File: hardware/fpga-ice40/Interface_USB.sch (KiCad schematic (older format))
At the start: 16 parts, among them J5 USB_B_Micro, U11 USBLC6-2SC6, U9 FT245RL

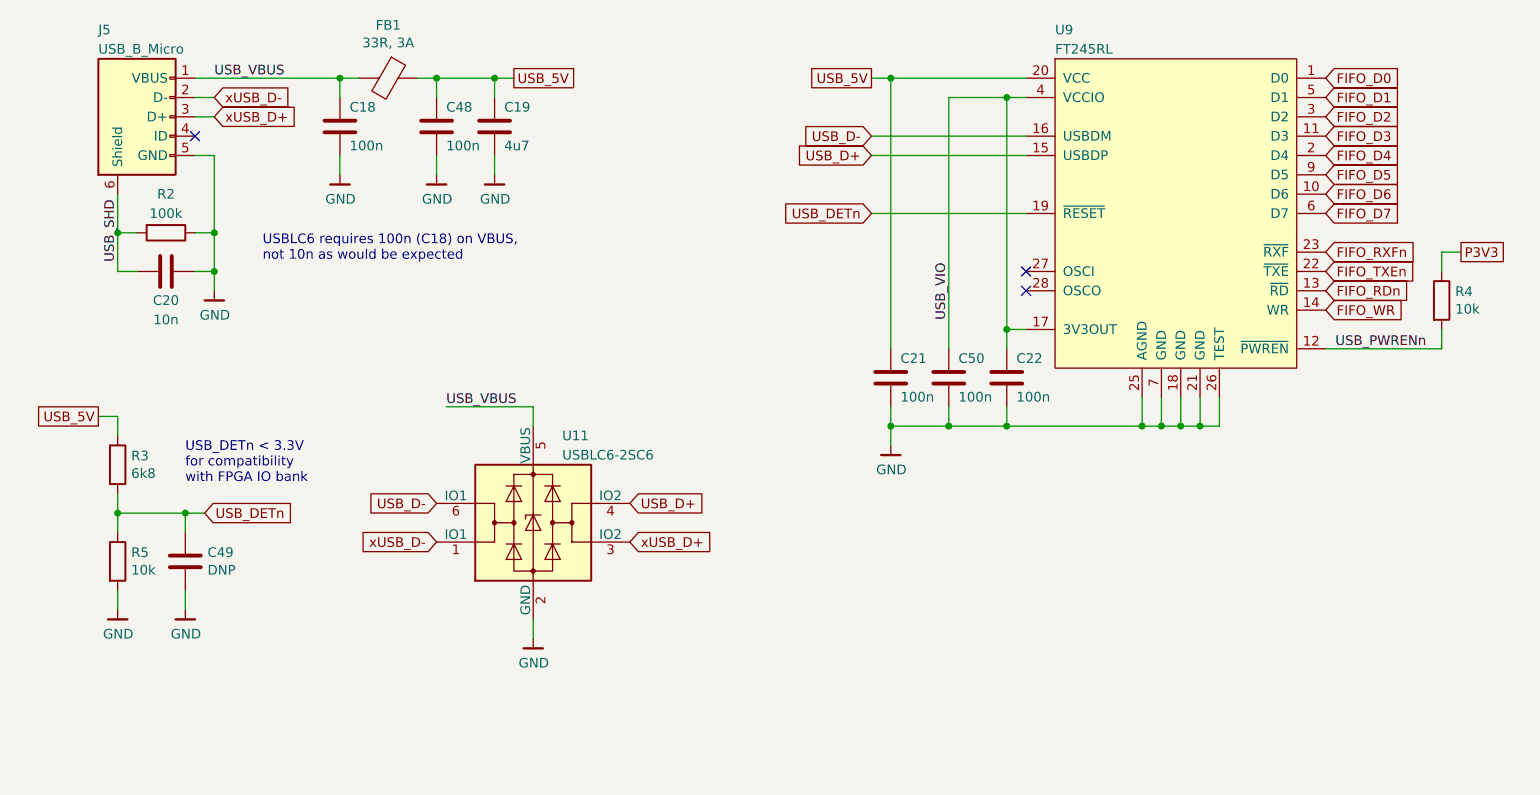
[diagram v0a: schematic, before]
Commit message: Beginning layout of power muxing module
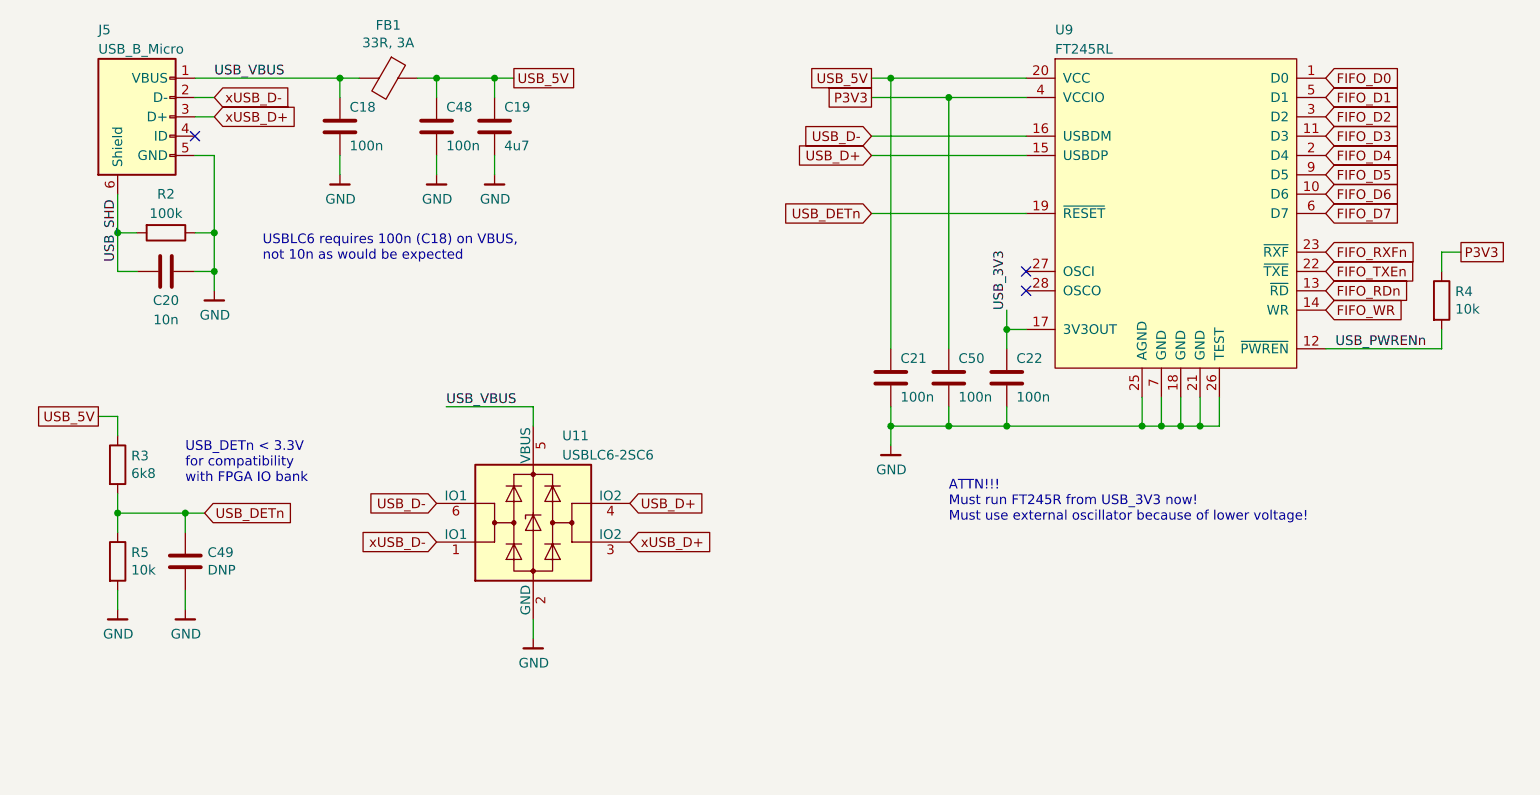
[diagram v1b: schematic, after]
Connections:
- net P3V3: now also C50.1, U9.4 (VCCIO)
- net USB_VIO renamed USB_3V3
- net USB_3V3: no longer C50.1, U9.4 (VCCIO)
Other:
- note added: "ATTN!!!\nMust run FT245R from USB_3V3 now!\nMust use external oscillator because of lower voltage!"
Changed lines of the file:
@@
 Wire Wire Line
 	8000 4250 8100 4250
-$Comp
-L ng_power:GND #PWR?
-U 1 1 5F314866
-P 6400 4350
-AR Path="/5F314866" Ref="#PWR?"  Part="1"
-AR Path="/5F302051/5F314866" Ref="#PWR025"  Part="1"
-F 0 "#PWR025" H 6400 4100 50  0001 C CNN
-F 1 "GND" H 6403 4224 50  0000 C CNN
-F 2 "" H 6300 4000 50  0001 C CNN
-F 3 "" H 6400 4350 50  0001 C CNN
-	1    6400 4350
-	1    0    0    -1
-$EndComp
-Wire Wire Line
-	6400 4350 6400 4250
 NoConn ~ 7100 3450
 NoConn ~ 7100 3550
@@
 	1    0    0    -1
 $EndComp
-Text GLabel 6300 2750 0    50   Input ~ 0
-USB_D-
-Text GLabel 6300 2850 0    50   Input ~ 0
-USB_D+
 Text GLabel 8650 2450 2    50   Input ~ 0
 FIFO_D0
@@
 Wire Wire Line
 	9250 3450 9250 3350
-Wire Wire Line
-	7000 2550 7100 2550
 Text GLabel 9350 3350 2    50   UnSpc ~ 0
 P3V3
 Wire Wire Line
 	9250 3350 9350 3350
-Wire Wire Line
-	7000 3750 7000 2550
-Connection ~ 7000 3750
-Wire Wire Line
-	6300 2750 7100 2750
-Wire Wire Line
-	6300 2850 7100 2850
-Wire Wire Line
-	6300 2450 6400 2450
-Text GLabel 6300 2450 0    50   UnSpc ~ 0
-USB_5V
-Wire Wire Line
-	6300 3150 7100 3150
-Text GLabel 6300 3150 0    50   Input ~ 0
-USB_DETn
-Text Label 6700 3700 1    50   ~ 0
-USB_VIO
 Text Label 8700 3850 0    50   ~ 0
 USB_PWRENn
@@
 Text GLabel 2850 4700 2    50   Input ~ 0
 USB_DETn
-$Comp
-L Device:C C?
-U 1 1 5F3148C7
-P 6400 4000
-AR Path="/5F3148C7" Ref="C?"  Part="1"
-AR Path="/5F302051/5F3148C7" Ref="C21"  Part="1"
-F 0 "C21" H 6450 4100 50  0000 L CNN
-F 1 "100n" H 6450 3900 50  0000 L CNN
-F 2 "Capacitor_SMD:C_0603_1608Metric" H 6438 3850 50  0001 C CNN
-F 3 "~" H 6400 4000 50  0001 C CNN
-F 4 "CL10B104KB8NNNC" H 6400 4000 50  0001 C CNN "MPN"
-	1    6400 4000
-	1    0    0    -1
-$EndComp
-Wire Wire Line
-	6400 3850 6400 2450
-Connection ~ 6400 2450
-Wire Wire Line
-	6400 2450 7100 2450
-Wire Wire Line
-	6400 4150 6400 4250
-Wire Wire Line
-	6400 4250 6700 4250
-Connection ~ 6400 4250
 Wire Wire Line
 	7000 4250 7700 4250
@@
 	1    0    0    -1
 $EndComp
+Wire Wire Line
+	6700 2550 7100 2550
+Connection ~ 7000 4250
+Wire Wire Line
+	6700 3850 6700 2550
+Wire Wire Line
+	6700 4250 7000 4250
+Wire Wire Line
+	6700 4150 6700 4250
 $Comp
 L Device:C C?
@@
 	1    0    0    -1
 $EndComp
-Connection ~ 7000 4250
-Wire Wire Line
-	6700 4150 6700 4250
+Connection ~ 6700 2550
 Connection ~ 6700 4250
 Wire Wire Line
-	6700 4250 7000 4250
-Wire Wire Line
-	6700 3850 6700 2550
-Wire Wire Line
-	6700 2550 7000 2550
-Connection ~ 7000 2550
+	6300 2550 6700 2550
+Text GLabel 6300 2550 0    50   UnSpc ~ 0
+P3V3
+Connection ~ 6400 4250
+Wire Wire Line
+	6400 4250 6700 4250
+Wire Wire Line
+	6400 4150 6400 4250
+Wire Wire Line
+	6400 2450 7100 2450
+Connection ~ 6400 2450
+Wire Wire Line
+	6400 3850 6400 2450
+$Comp
+L Device:C C?
+U 1 1 5F3148C7
+P 6400 4000
+AR Path="/5F3148C7" Ref="C?"  Part="1"
+AR Path="/5F302051/5F3148C7" Ref="C21"  Part="1"
+F 0 "C21" H 6450 4100 50  0000 L CNN
+F 1 "100n" H 6450 3900 50  0000 L CNN
+F 2 "Capacitor_SMD:C_0603_1608Metric" H 6438 3850 50  0001 C CNN
+F 3 "~" H 6400 4000 50  0001 C CNN
+F 4 "CL10B104KB8NNNC" H 6400 4000 50  0001 C CNN "MPN"
+	1    6400 4000
+	1    0    0    -1
+$EndComp
+Text GLabel 6300 2450 0    50   UnSpc ~ 0
+USB_5V
+Wire Wire Line
+	6300 2450 6400 2450
+Wire Wire Line
+	6400 4350 6400 4250
+$Comp
+L ng_power:GND #PWR?
+U 1 1 5F314866
+P 6400 4350
+AR Path="/5F314866" Ref="#PWR?"  Part="1"
+AR Path="/5F302051/5F314866" Ref="#PWR025"  Part="1"
+F 0 "#PWR025" H 6400 4100 50  0001 C CNN
+F 1 "GND" H 6403 4224 50  0000 C CNN
+F 2 "" H 6300 4000 50  0001 C CNN
+F 3 "" H 6400 4350 50  0001 C CNN
+	1    6400 4350
+	1    0    0    -1
+$EndComp
+Text Label 7000 3650 1    50   ~ 0
+USB_3V3
+Wire Wire Line
+	6300 3150 7100 3150
+Text GLabel 6300 3150 0    50   Input ~ 0
+USB_DETn
+Wire Wire Line
+	6300 2850 7100 2850
+Text GLabel 6300 2850 0    50   Input ~ 0
+USB_D+
+Wire Wire Line
+	6300 2750 7100 2750
+Text GLabel 6300 2750 0    50   Input ~ 0
+USB_D-
+Wire Wire Line
+	7000 3650 7000 3750
+Connection ~ 7000 3750
+Text Notes 6700 4750 0    50   ~ 0
+ATTN!!!\nMust run FT245R from USB_3V3 now!\nMust use external oscillator because of lower voltage!
 $EndSCHEMATC

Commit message: Swtich USB interface to P3V3 and add 12MHz oscillator
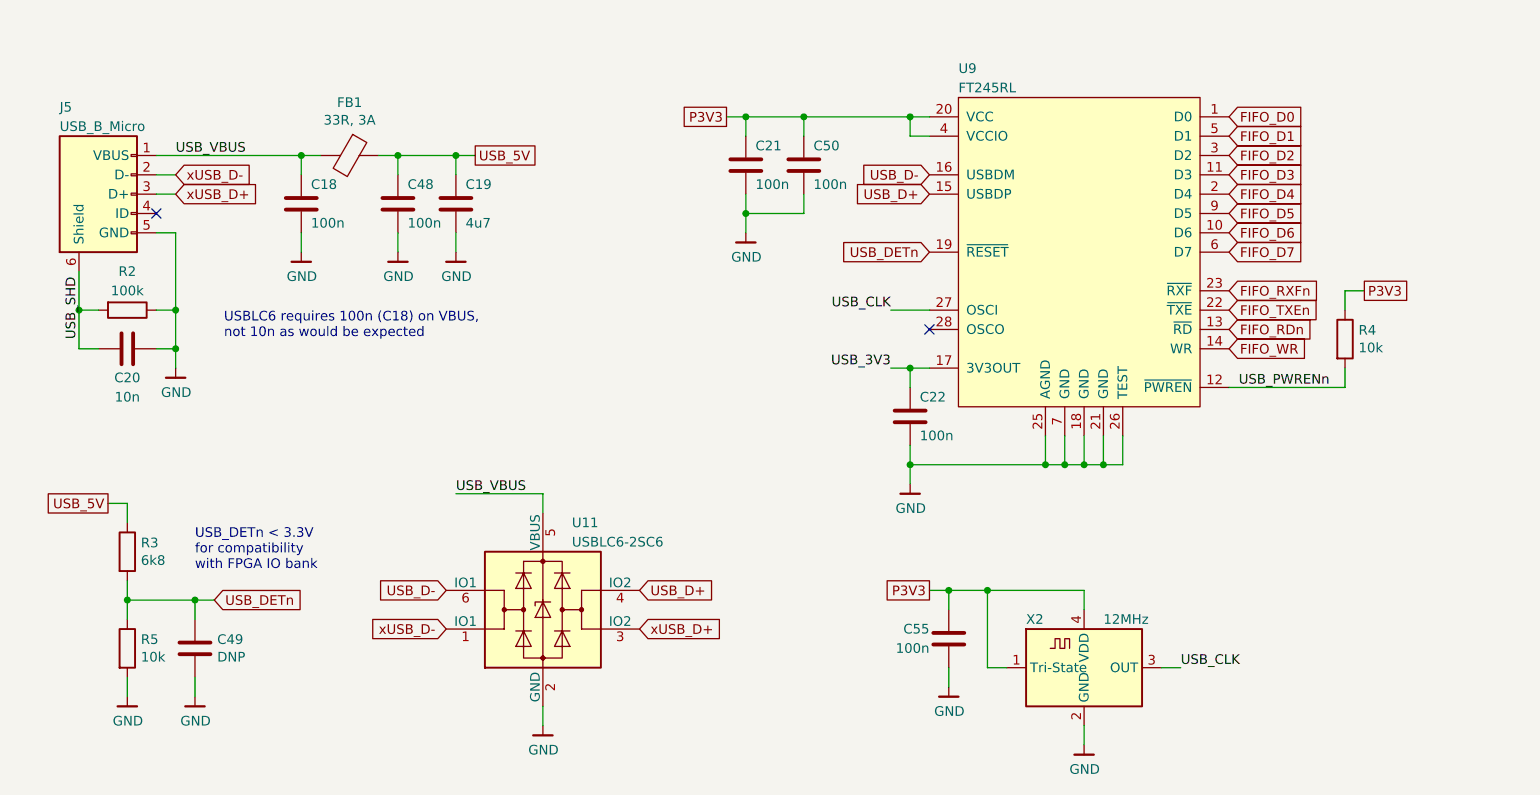
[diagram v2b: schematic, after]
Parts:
- added C55: 100n, Capacitor_SMD:C_0603_1608Metric, symbol Device:C
- added X2: 12MHz, ng_time:Oscillator_2.5x2.0, symbol Oscillator:ECS-2520MV-xxx-xx
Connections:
- net GND: now also C55.2, X2.2 (GND)
- net P3V3: now also C21.1, U9.20 (VCC), C55.1, X2.1 (Tri-State), X2.4 (VDD)
- net USB_5V: no longer C21.1, U9.20 (VCC)
- net USB_CLK: now reaches U9.27 (OSCI)
- net USB_CLK: now also X2.3 (OUT)
- no-connect marks 3 -> 2
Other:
- note removed: "ATTN!!!\nMust run FT245R from USB_3V3 now!\nMust use external oscillator because of lower voltage!"
- moved on the sheet: C18, C19, C20, C21, C22, C48, C49, C50, FB1, J5, R2, R3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
